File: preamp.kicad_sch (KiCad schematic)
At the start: 18 parts, among them Q1 2N3904, Q2 2N3904

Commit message: Actualización de esquemáticos
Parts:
- R1, R1*, R2, R3, R4, R5, R6, R7, R8, R9: footprint (none) -> Resistor_THT:R_Axial_DIN0207_L6.3mm_D2.5mm_P7.62mm_Horizontal
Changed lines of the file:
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@@
 (kicad_sch
-	(version 20231120)
+	(version 20250114)
 	(generator "eeschema")
-	(generator_version "8.0")
+	(generator_version "9.0")
 	(paper "A4")
 	(junction
@@
 			)
 		)
-		(property "Footprint" ""
+		(property "Footprint" "Resistor_THT:R_Axial_DIN0207_L6.3mm_D2.5mm_P7.62mm_Horizontal"
 			(at 112.268 104.14 90)
 			(effects
@@
 			)
 		)
-		(property "Footprint" ""
+		(property "Footprint" "Resistor_THT:R_Axial_DIN0207_L6.3mm_D2.5mm_P7.62mm_Horizontal"
 			(at 154.178 104.14 90)
 			(effects
@@
 			)
 		)
-		(property "Footprint" ""
+		(property "Footprint" "Resistor_THT:R_Axial_DIN0207_L6.3mm_D2.5mm_P7.62mm_Horizontal"
 			(at 132.588 74.93 90)
 			(effects
@@
 			)
 		)
-		(property "Footprint" ""
+		(property "Footprint" "Resistor_THT:R_Axial_DIN0207_L6.3mm_D2.5mm_P7.62mm_Horizontal"
 			(at 74.422 96.52 90)
 			(effects
@@
 			)
 		)
-		(property "Footprint" ""
+		(property "Footprint" "Resistor_THT:R_Axial_DIN0207_L6.3mm_D2.5mm_P7.62mm_Horizontal"
 			(at 187.198 116.84 90)
 			(effects
@@
 			)
 		)
-		(property "Footprint" ""
+		(property "Footprint" "Resistor_THT:R_Axial_DIN0207_L6.3mm_D2.5mm_P7.62mm_Horizontal"
 			(at 132.588 104.14 90)
 			(effects
@@
 			)
 		)
-		(property "Footprint" ""
+		(property "Footprint" "Resistor_THT:R_Axial_DIN0207_L6.3mm_D2.5mm_P7.62mm_Horizontal"
 			(at 122.428 104.14 90)
 			(effects
@@
 			)
 		)
-		(property "Footprint" ""
+		(property "Footprint" "Resistor_THT:R_Axial_DIN0207_L6.3mm_D2.5mm_P7.62mm_Horizontal"
 			(at 101.6 87.122 90)
 			(effects
@@
 			)
 		)
-		(property "Footprint" ""
+		(property "Footprint" "Resistor_THT:R_Axial_DIN0207_L6.3mm_D2.5mm_P7.62mm_Horizontal"
 			(at 164.338 116.84 90)
 			(effects
@@
 			)
 		)
-		(property "Footprint" ""
+		(property "Footprint" "Resistor_THT:R_Axial_DIN0207_L6.3mm_D2.5mm_P7.62mm_Horizontal"
 			(at 144.018 104.14 90)
 			(effects

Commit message: Actualización esquemáticos
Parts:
- renumbered R1* to R101
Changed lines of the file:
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@@
 			)
 		)
-		(property "Description" ""
+		(property "Description" "Power symbol creates a global label with name \"GND\" , ground"
 			(at 120.65 109.22 0)
 			(effects
@@
 			)
 		)
-		(property "Description" ""
+		(property "Description" "Power symbol creates a global label with name \"VCC\""
 			(at 130.81 66.04 0)
 			(effects
@@
 			)
 		)
-		(property "Description" ""
+		(property "Description" "Power symbol creates a global label with name \"GND\" , ground"
 			(at 152.4 109.22 0)
 			(effects
@@
 		(dnp no)
 		(fields_autoplaced yes)
-		(property "Reference" "R1*"
+		(property "Reference" "R101"
 			(at 78.74 95.2499 0)
 			(effects
@@
 			(project "test"
 				(path "/6df9a4de-ce35-4607-9a42-d3c459c15494/5b01a279-c198-4a64-a80f-c0e252d1dee4"
-					(reference "R1*")
+					(reference "R101")
 					(unit 1)
 				)
@@
 			)
 		)
-		(property "Description" ""
+		(property "Description" "Power symbol creates a global label with name \"GND\" , ground"
 			(at 185.42 121.92 0)
 			(effects
@@
 			)
 		)
-		(property "Description" ""
+		(property "Description" "0.2A Ic, 40V Vce, Small Signal NPN Transistor, TO-92"
 			(at 149.86 88.9 0)
 			(effects
@@
 			)
 		)
-		(property "Description" ""
+		(property "Description" "0.2A Ic, 40V Vce, Small Signal NPN Transistor, TO-92"
 			(at 128.27 88.9 0)
 			(effects
@@
 			)
 		)
-		(property "Description" ""
+		(property "Description" "Power symbol creates a global label with name \"GND\" , ground"
 			(at 130.81 109.22 0)
 			(effects
@@
 	)
 	(symbol
+		(lib_name "GND_1")
 		(lib_id "power:GND")
 		(at 76.2 102.87 0)
@@
 			)
 		)
-		(property "Description" ""
+		(property "Description" "Power symbol creates a global label with name \"GND\" , ground"
 			(at 76.2 102.87 0)
 			(effects
@@
 			)
 		)
-		(property "Description" ""
+		(property "Description" "Power symbol creates a global label with name \"GND\" , ground"
 			(at 142.24 134.62 0)
 			(effects

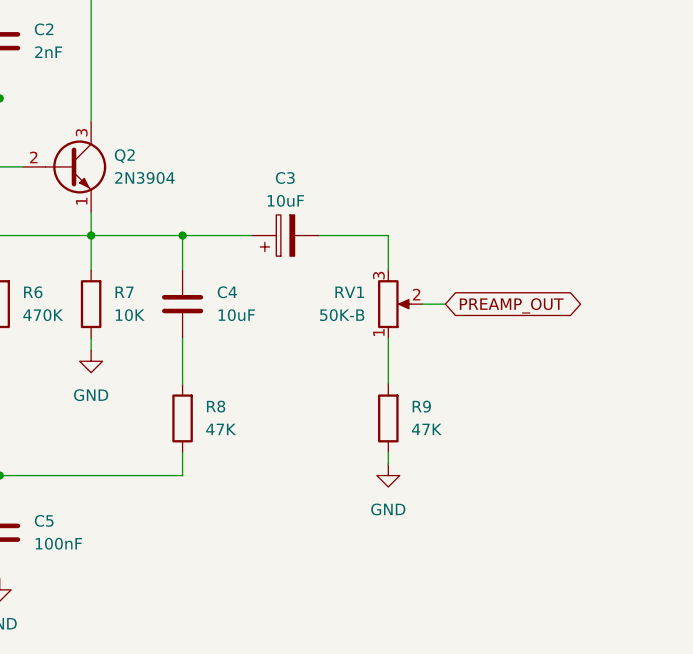
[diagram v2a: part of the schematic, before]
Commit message: Asignación de huellas a componentes.
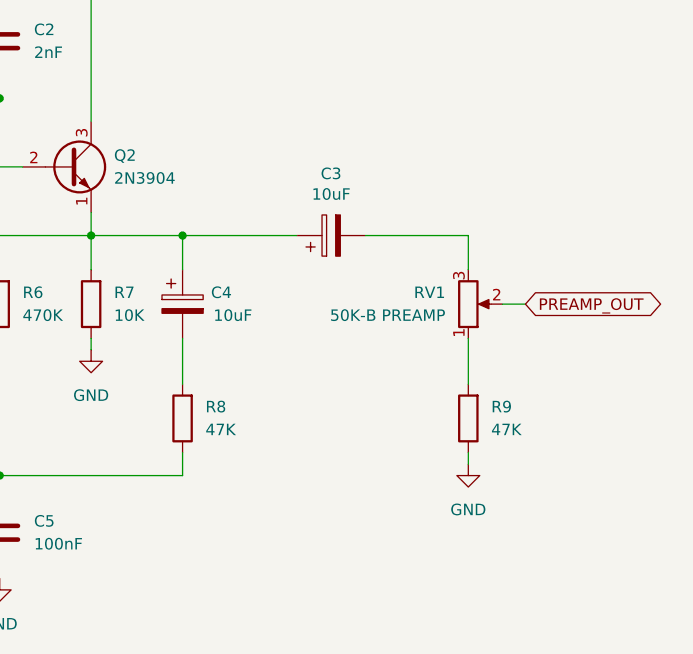
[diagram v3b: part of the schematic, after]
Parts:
- removed C4: 10uF, symbol Device:C
- added C4: 10uF, Capacitor_THT:CP_Radial_D5.0mm_P2.00mm, symbol Device:C_Polarized
- C1, C3: footprint (none) -> Capacitor_THT:CP_Radial_D5.0mm_P2.00mm
- C2, C5: footprint (none) -> Capacitor_THT:C_Disc_D5.1mm_W3.2mm_P5.00mm
- RV1: value 50K-B -> 50K-B PREAMP; footprint (none) -> DIY_jorge:Pot Alpha 16mm
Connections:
- net at C3.1, Q2.1 (E), R6.2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: now also C4.1
- net at R8.2: now also C4.2
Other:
- moved on the sheet: R9, RV1

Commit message: Archivos de Fabricación listos.
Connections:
- net GND: now also R9.2; no longer R9.1
- net at RV1.1: now also R9.1; no longer R9.2
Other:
- moved on the sheet: R9
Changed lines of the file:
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@@
 	(symbol
 		(lib_id "Device:R")
-		(at 194.31 116.84 180)
+		(at 194.31 116.84 0)
 		(unit 1)
 		(exclude_from_sim no)
@@
 		(fields_autoplaced yes)
 		(property "Reference" "R9"
-			(at 196.85 115.57 0)
+			(at 196.85 115.5699 0)
 			(effects
 				(font
 					(size 1.27 1.27)
 				)
-				(justify right)
+				(justify left)
 			)
 		)
 		(property "Value" "47K"
-			(at 196.85 118.11 0)
+			(at 196.85 118.1099 0)
 			(effects
 				(font
 					(size 1.27 1.27)
 				)
-				(justify right)
+				(justify left)
 			)
 		)
 		(property "Footprint" "Resistor_THT:R_Axial_DIN0207_L6.3mm_D2.5mm_P7.62mm_Horizontal"
-			(at 196.088 116.84 90)
+			(at 192.532 116.84 90)
 			(effects
 				(font
